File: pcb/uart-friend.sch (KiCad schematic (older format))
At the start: 22 parts, among them P1 USB_OTG, P3 CONN_01X03, P4 CONN_01X03, P5 CONN_01X06, P6 CONN_01X03, Q1 Q_PMOS_GSD, U1 AP7365_ADJ_SOT-23-5, U2 CY7C65213-SSOP

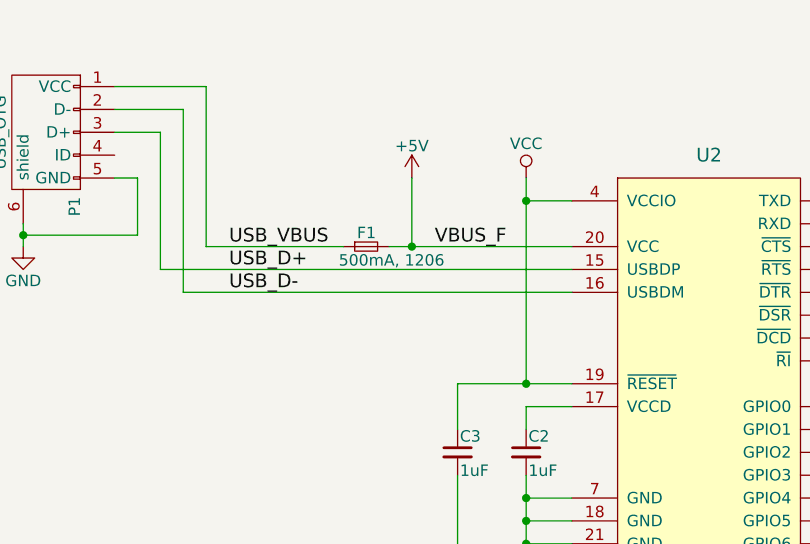
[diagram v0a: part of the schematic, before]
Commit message: make single board gerbers, placement, and bom
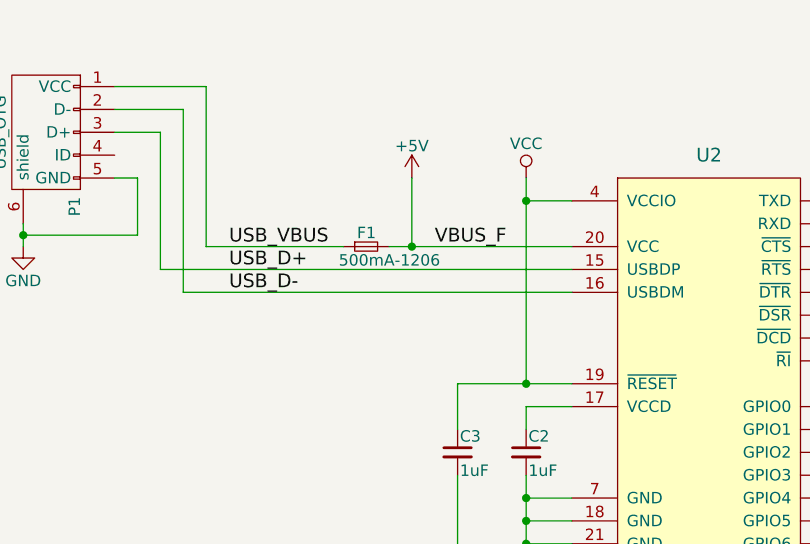
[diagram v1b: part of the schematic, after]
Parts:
- F1: value 500mA, 1206 -> 500mA-1206
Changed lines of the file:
@@
 $EndComp
 $Comp
-L GND #PWR3
+L GND #PWR01
 U 1 1 56F1DB58
 P 3550 7000
-F 0 "#PWR3" H 3550 6750 50  0001 C CNN
+F 0 "#PWR01" H 3550 6750 50  0001 C CNN
 F 1 "GND" H 3550 6850 50  0000 C CNN
 F 2 "" H 3550 7000 50  0000 C CNN
@@
 FB_1V8
 $Comp
-L GND #PWR1
+L GND #PWR02
 U 1 1 56F1E578
 P 1900 2600
-F 0 "#PWR1" H 1900 2350 50  0001 C CNN
+F 0 "#PWR02" H 1900 2350 50  0001 C CNN
 F 1 "GND" H 1900 2450 50  0000 C CNN
 F 2 "" H 1900 2600 50  0000 C CNN
@@
 $EndComp
 $Comp
-L +5V #PWR2
+L +5V #PWR03
 U 1 1 56F1E5AF
 P 2000 5500
-F 0 "#PWR2" H 2000 5350 50  0001 C CNN
+F 0 "#PWR03" H 2000 5350 50  0001 C CNN
 F 1 "+5V" H 2000 5640 50  0000 C CNN
 F 2 "" H 2000 5500 50  0000 C CNN
@@
 	2700 1900 2300 1900
 $Comp
-L +5V #PWR4
+L +5V #PWR04
 U 1 1 56F1EB0B
 P 3600 2300
-F 0 "#PWR4" H 3600 2150 50  0001 C CNN
+F 0 "#PWR04" H 3600 2150 50  0001 C CNN
 F 1 "+5V" H 3600 2440 50  0000 C CNN
 F 2 "" H 3600 2300 50  0000 C CNN
@@
 $EndComp
 $Comp
-L VCC #PWR5
+L VCC #PWR05
 U 1 1 56F1EB97
 P 4100 2300
-F 0 "#PWR5" H 4100 2150 50  0001 C CNN
+F 0 "#PWR05" H 4100 2150 50  0001 C CNN
 F 1 "VCC" H 4100 2450 50  0000 C CNN
 F 2 "" H 4100 2300 50  0000 C CNN
@@
 	4100 2400 4300 2400
 $Comp
-L VCC #PWR7
+L VCC #PWR06
 U 1 1 56F1EC9B
 P 4400 5500
-F 0 "#PWR7" H 4400 5350 50  0001 C CNN
+F 0 "#PWR06" H 4400 5350 50  0001 C CNN
 F 1 "VCC" H 4400 5650 50  0000 C CNN
 F 2 "" H 4400 5500 50  0000 C CNN
@@
 	2000 5500 2000 6300
 $Comp
-L GND #PWR6
+L GND #PWR07
 U 1 1 56F1EF7F
 P 4100 4100
-F 0 "#PWR6" H 4100 3850 50  0001 C CNN
+F 0 "#PWR07" H 4100 3850 50  0001 C CNN
 F 1 "GND" H 4100 3950 50  0000 C CNN
 F 2 "" H 4100 4100 50  0000 C CNN
@@
 	6800 2400 6300 2400
 $Comp
-L GND #PWR11
+L GND #PWR08
 U 1 1 56F1FC9D
 P 6900 1700
-F 0 "#PWR11" H 6900 1450 50  0001 C CNN
+F 0 "#PWR08" H 6900 1450 50  0001 C CNN
 F 1 "GND" H 6900 1550 50  0000 C CNN
 F 2 "" H 6900 1700 50  0000 C CNN
@@
 	6500 3500 6300 3500
 $Comp
-L VCC #PWR12
+L VCC #PWR09
 U 1 1 56F25F52
 P 7000 3200
-F 0 "#PWR12" H 7000 3050 50  0001 C CNN
+F 0 "#PWR09" H 7000 3050 50  0001 C CNN
 F 1 "VCC" H 7000 3350 50  0000 C CNN
 F 2 "" H 7000 3200 50  0000 C CNN
@@
 P 3400 2600
 F 0 "F1" H 3360 2660 50  0000 L CNN
-F 1 "500mA, 1206" H 3280 2540 50  0000 L CNN
+F 1 "500mA-1206" H 3280 2540 50  0000 L CNN
 F 2 "Fuse_Holders_and_Fuses:Fuse_SMD1206_Reflow" H 3400 2600 50  0001 C CNN
 F 3 "" H 3400 2600 50  0000 C CNN
@@
 Target Power\nSource Select
 $Comp
-L +5V #PWR10
+L +5V #PWR010
 U 1 1 56F27552
 P 6500 4900
-F 0 "#PWR10" H 6500 4750 50  0001 C CNN
+F 0 "#PWR010" H 6500 4750 50  0001 C CNN
 F 1 "+5V" H 6500 5040 50  0000 C CNN
 F 2 "" H 6500 4900 50  0000 C CNN
@@
 	6500 5000 6500 4900
 $Comp
-L +5V #PWR8
+L +5V #PWR011
 U 1 1 56F27756
 P 4700 5500
-F 0 "#PWR8" H 4700 5350 50  0001 C CNN
+F 0 "#PWR011" H 4700 5350 50  0001 C CNN
 F 1 "+5V" H 4700 5640 50  0000 C CNN
 F 2 "" H 4700 5500 50  0000 C CNN
@@
 Connection ~ 7000 3500
 $Comp
-L GND #PWR9
+L GND #PWR012
 U 1 1 56F872F9
 P 5900 3850
-F 0 "#PWR9" H 5900 3600 50  0001 C CNN
+F 0 "#PWR012" H 5900 3600 50  0001 C CNN
 F 1 "GND" H 5900 3700 50  0000 C CNN
 F 2 "" H 5900 3850 50  0000 C CNN
